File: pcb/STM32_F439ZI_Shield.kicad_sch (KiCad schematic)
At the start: 7 parts, among them U1 Opamp_Dual

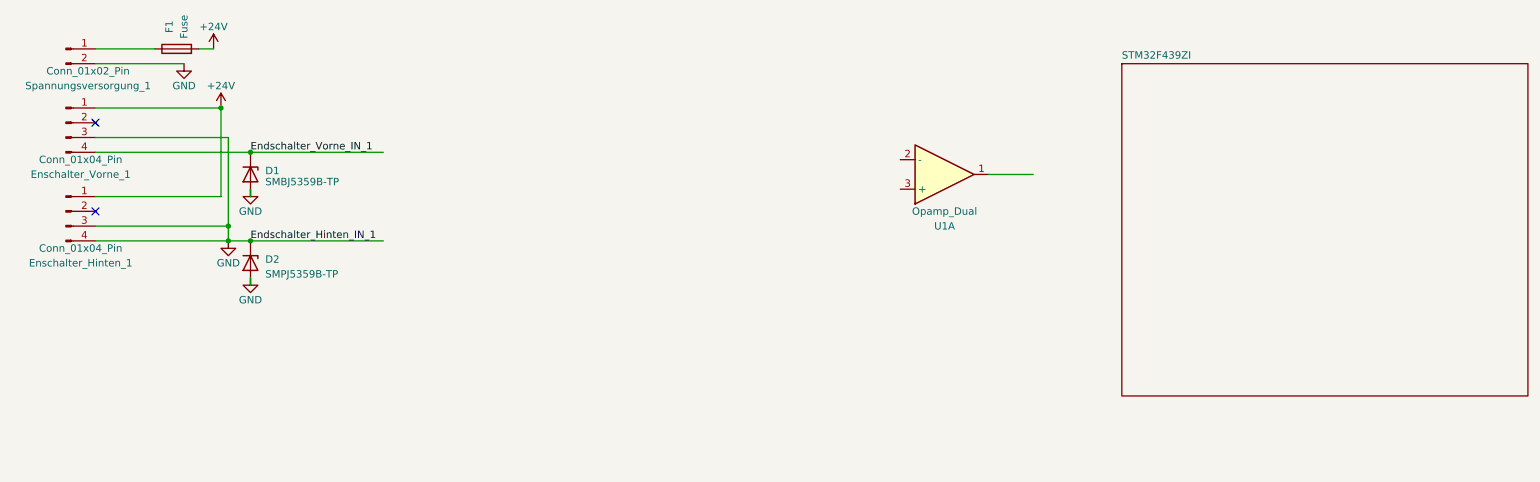
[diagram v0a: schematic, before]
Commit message: added Subsheets vor different component types
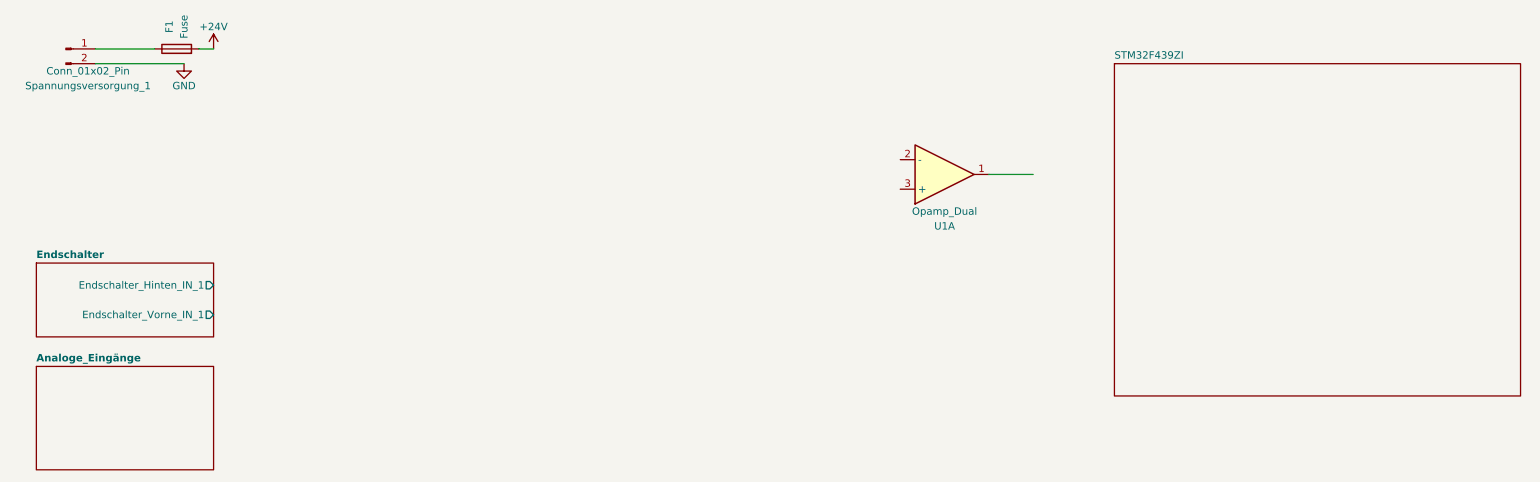
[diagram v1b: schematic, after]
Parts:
- removed D1: SMBJ5359B-TP, Diode_SMD:D_SMB, symbol Diode:Z2SMBxxx
- removed D2: SMPJ5359B-TP, Diode_SMD:D_SMB, symbol Diode:Z2SMBxxx
- removed Enschalter_Hinten_1, Enschalter_Vorne_1: Conn_01x04_Pin, symbol Connector:Conn_01x04_Pin
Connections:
- no-connect marks 2 -> 0
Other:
- added sheet Analoge_Eingänge (analog_in.kicad_sch)
- added sheet Endschalter (Endschalter.kicad_sch)

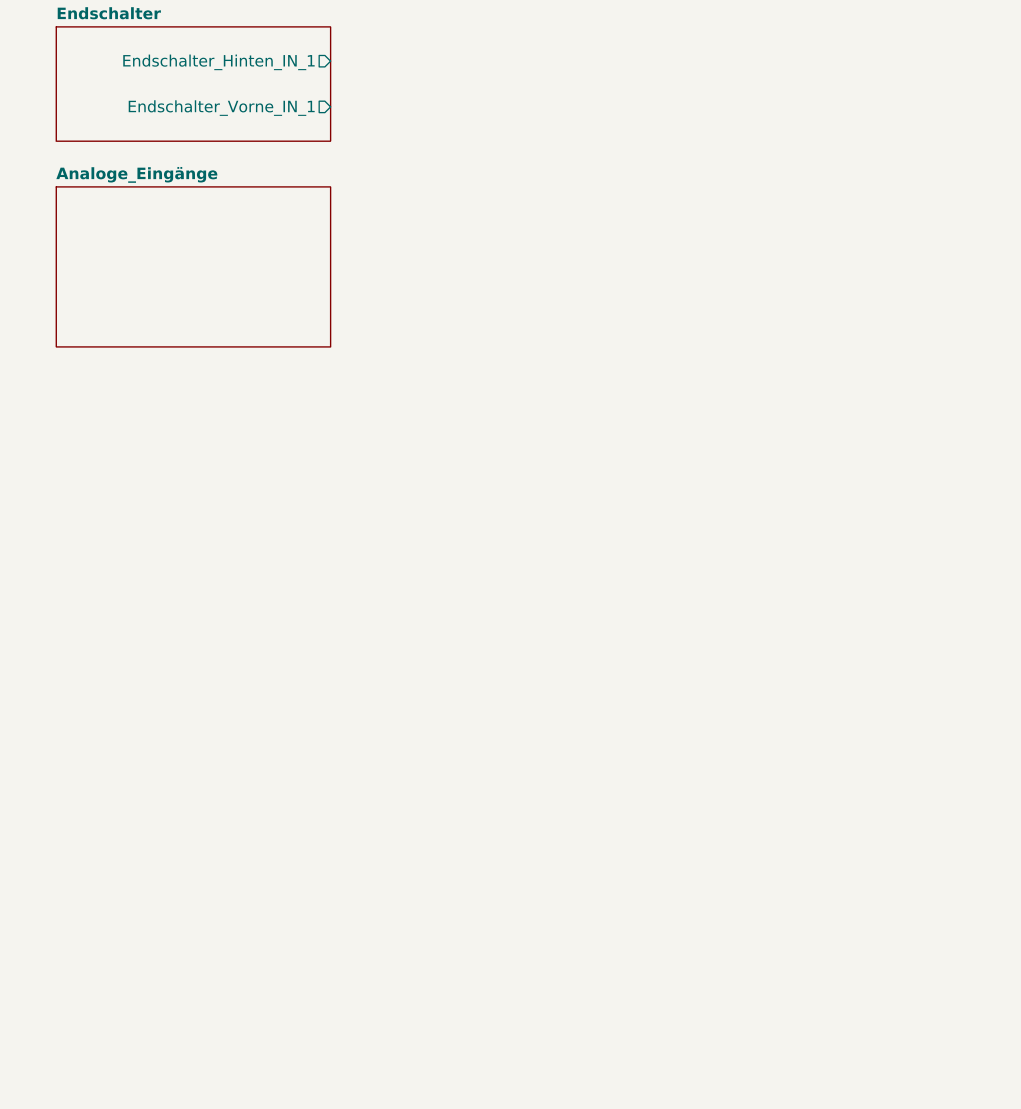
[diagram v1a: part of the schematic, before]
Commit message: added new sheet and added sensors
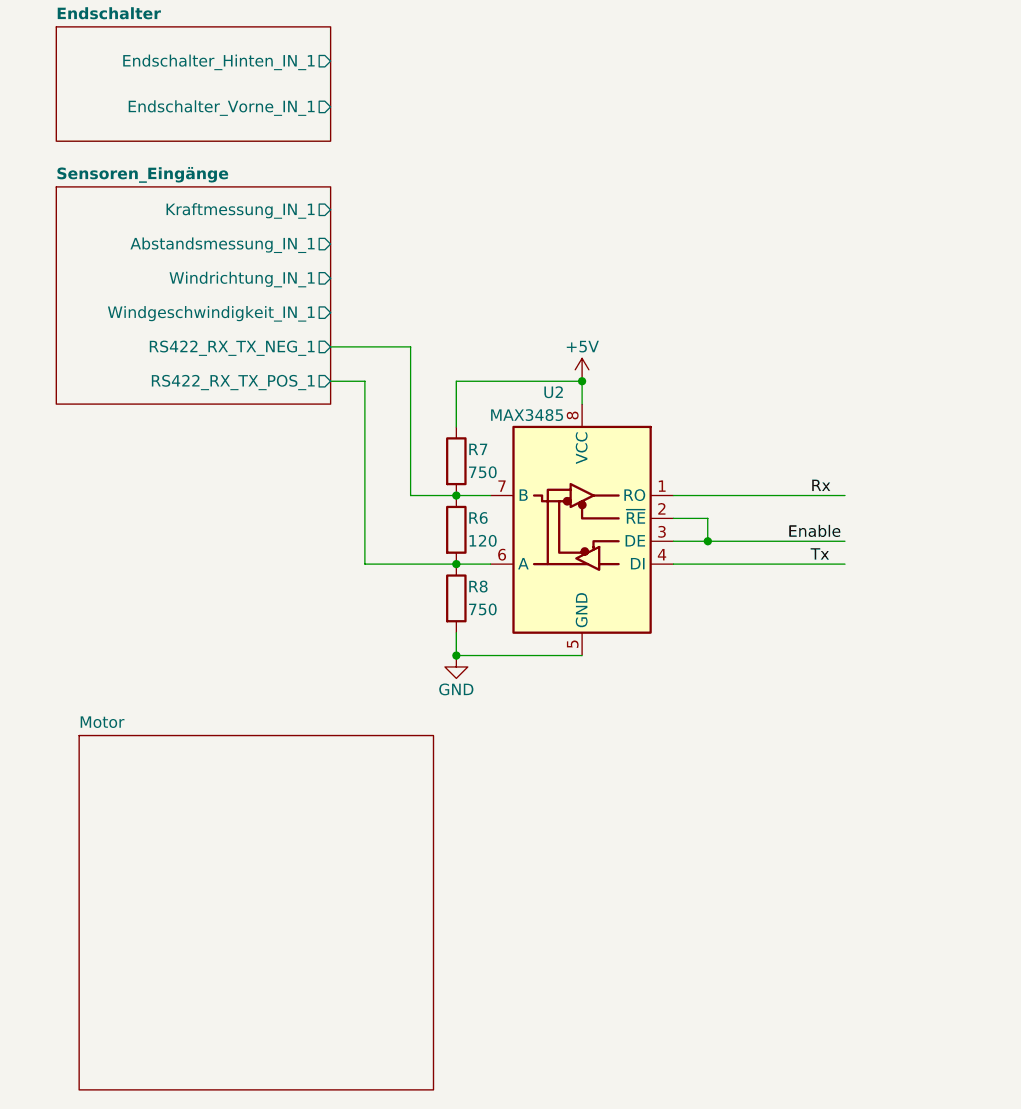
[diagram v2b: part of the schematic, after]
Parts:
- added R6: 120, Resistor_SMD:R_0201_0603Metric, symbol Device:R
- added R7, R8: 750, Resistor_SMD:R_0201_0603Metric, symbol Device:R
- added U2: MAX3485, symbol Interface_UART:MAX3485
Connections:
- net GND: now also R8.2, U2.5 (GND)
- new net +5V: R7.1, U2.8 (VCC)
- new net Enable: U2.2 (~{RE}), U2.3 (DE)
- new net Rx: U2.1 (RO)
- new net Sensoren_Eingänge/RS422_RX_TX_NEG_1: R6.1, R7.2, U2.7 (B)
- new net Sensoren_Eingänge/RS422_RX_TX_POS_1: R6.2, R8.1, U2.6 (A)
- new net Tx: U2.4 (DI)
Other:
- sheet Analoge_Eingänge renamed Sensoren_Eingänge
- added sheet Motor (Motor.kicad_sch)
- sheet Sensoren_Eingänge ports: added Abstandsmessung_IN_1, Kraftmessung_IN_1, RS422_RX_TX_NEG_1, RS422_RX_TX_POS_1, Windgeschwindigkeit_IN_1, Windrichtung_IN_1; removed none

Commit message: Updated PCB
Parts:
- removed U1: Opamp_Dual, symbol Device:Opamp_Dual
- added C1: 22u, Capacitor_SMD:C_0603_1608Metric, symbol Device:C_Small
- added K1, K2: G6S-2, Relay_SMD:Relay_DPDT_Omron_G6S-2F, symbol Relay:G6S-2
- added R10: 240, Resistor_SMD:R_0603_1608Metric, symbol Device:R
- added R9: 10k, Resistor_SMD:R_0201_0603Metric, symbol Device:R
- added U1: LM2904, symbol Amplifier_Operational:LM2904
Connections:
- net Endschalter/Endschalter_Hinten_IN_1: now also K1.1
- net Endschalter/Endschalter_Vorne_IN_1: now also K2.1
- net GND: now also C1.2, K1.12, K2.12, R9.2, U1.4 (V-)
- net Sensoren_Eingänge/RS422_RX_TX_NEG_1 renamed Sensoren_Eingänge/RS485_RX_TX_NEG_1
- net Sensoren_Eingänge/RS422_RX_TX_POS_1 renamed Sensoren_Eingänge/RS485_RX_TX_POS_1
- new net: C1.1, R10.1, U1.3 (+)
- new net +3.3V: U1.8 (V+)
- new net Motor/Drehzahl_Analog_OUT: R9.1, U1.1, U1.2 (-)
- new net Optokoppler/IN0_MCU_IN: K2.4
- new net Optokoppler/IN1_MCU_IN: K1.4
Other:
- added sheet Optokoppler (untitled.kicad_sch)
- sheet Motor ports: added Drehzahl_Analog_OUT, IN0_OUT, IN1_OUT, IN2_OUT, IN3_OUT, OUT1_IN, OUT2_IN, OUT3_IN; removed none
- sheet Sensoren_Eingänge ports: added RS485_RX_TX_NEG_1, RS485_RX_TX_POS_1; removed RS422_RX_TX_NEG_1, RS422_RX_TX_POS_1

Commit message: updated pcb
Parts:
- added C2, C3, C4, C5, C6: 100p, Capacitor_SMD:C_0603_1608Metric, symbol Device:C_Small
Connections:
- net GND: now also C2.2, C3.2, C4.2, C5.2, C6.2
- net STM32F439ZI/IN0_MCU: now reaches K2.3
- net STM32F439ZI/IN1_MCU: now reaches K1.3
- net STM32F439ZI/Drehzahl_Analog_OUT: now reaches R10.2
- new net Motor/Stromsensor_MCU: C6.1
- new net STM32F439ZI/Abstandsmessung_MCU: C3.1
- new net STM32F439ZI/Kraftmessung_MCU: C2.1
- new net STM32F439ZI/Windgeschwindigkeit_MCU: C4.1
- new net STM32F439ZI/Windrichtung_MCU: C5.1
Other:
- sheet Motor ports: added Stromsensor_MCU; removed none
- sheet STM32F439ZI ports: added Abstandsmessung_MCU, Drehzahl_Analog_OUT, Endschalter_Hinten_MCU, Endschalter_Vorne_MCU, IN0_MCU, IN1_MCU, IN2_MCU, IN3_MCU, Kraftmessung_MCU, OUT1_MCU, OUT2_MCU, OUT3_MCU, Strommessung_MCU, UART_EN, UART_RX, UART_TX, Windgeschwindigkeit_MCU, Windrichtung_MCU; removed none
- moved on the sheet: C1, R10, R9, U1A, U1C

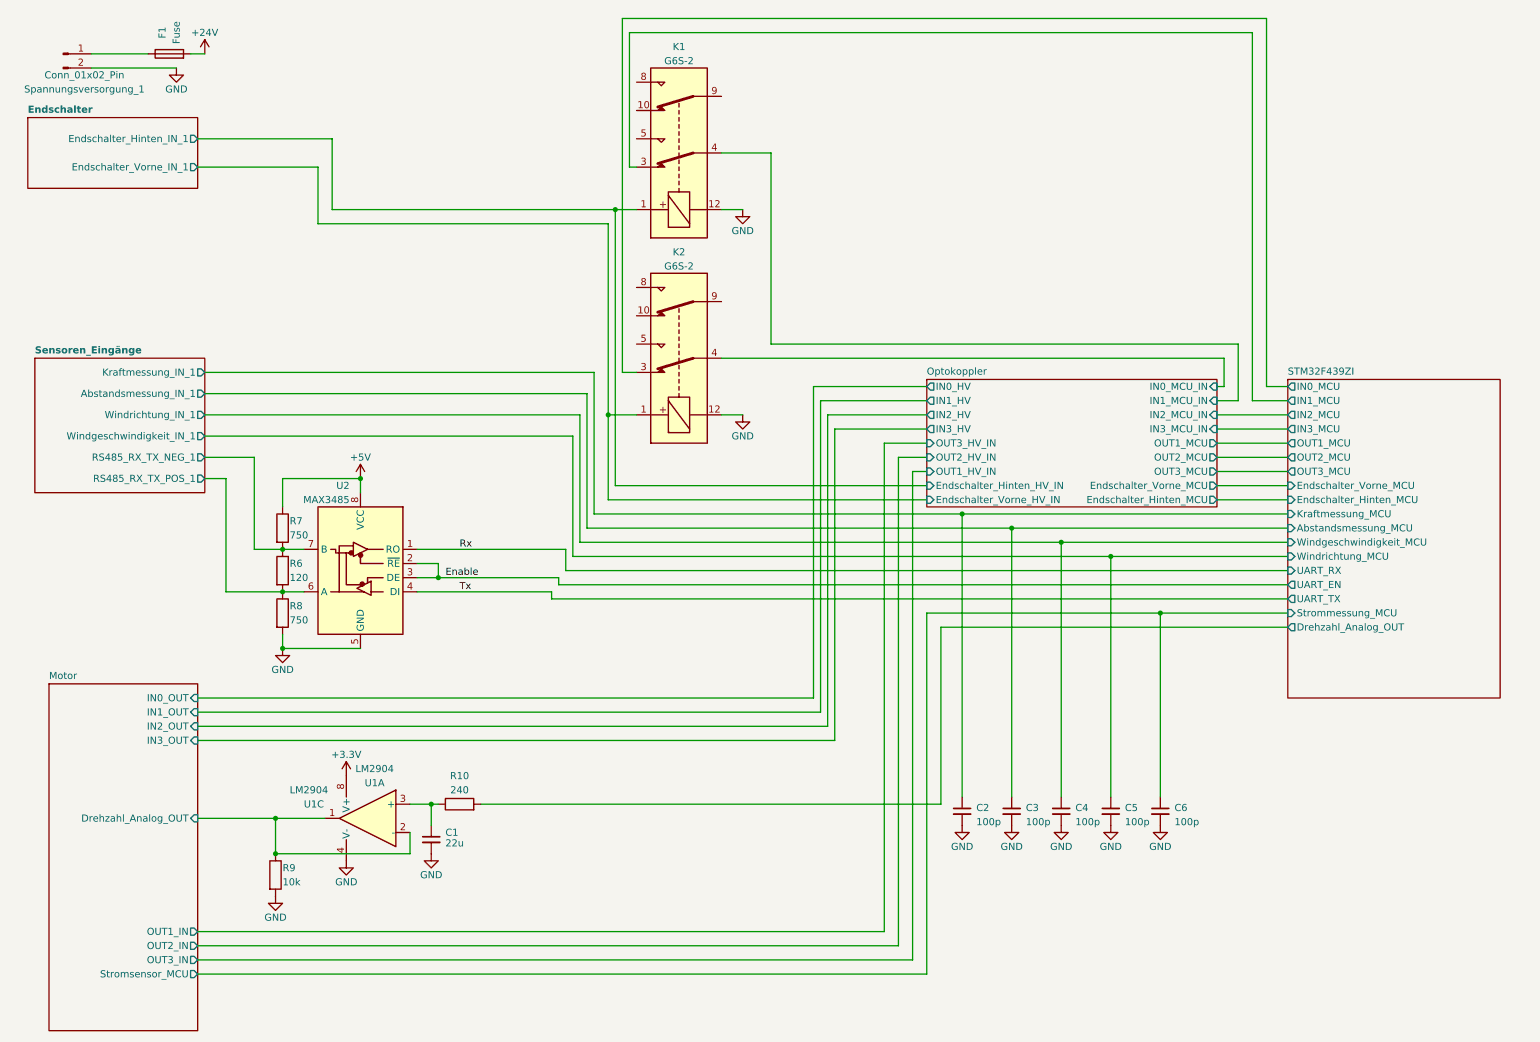
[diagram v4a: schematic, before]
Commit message: add dc/dc converter
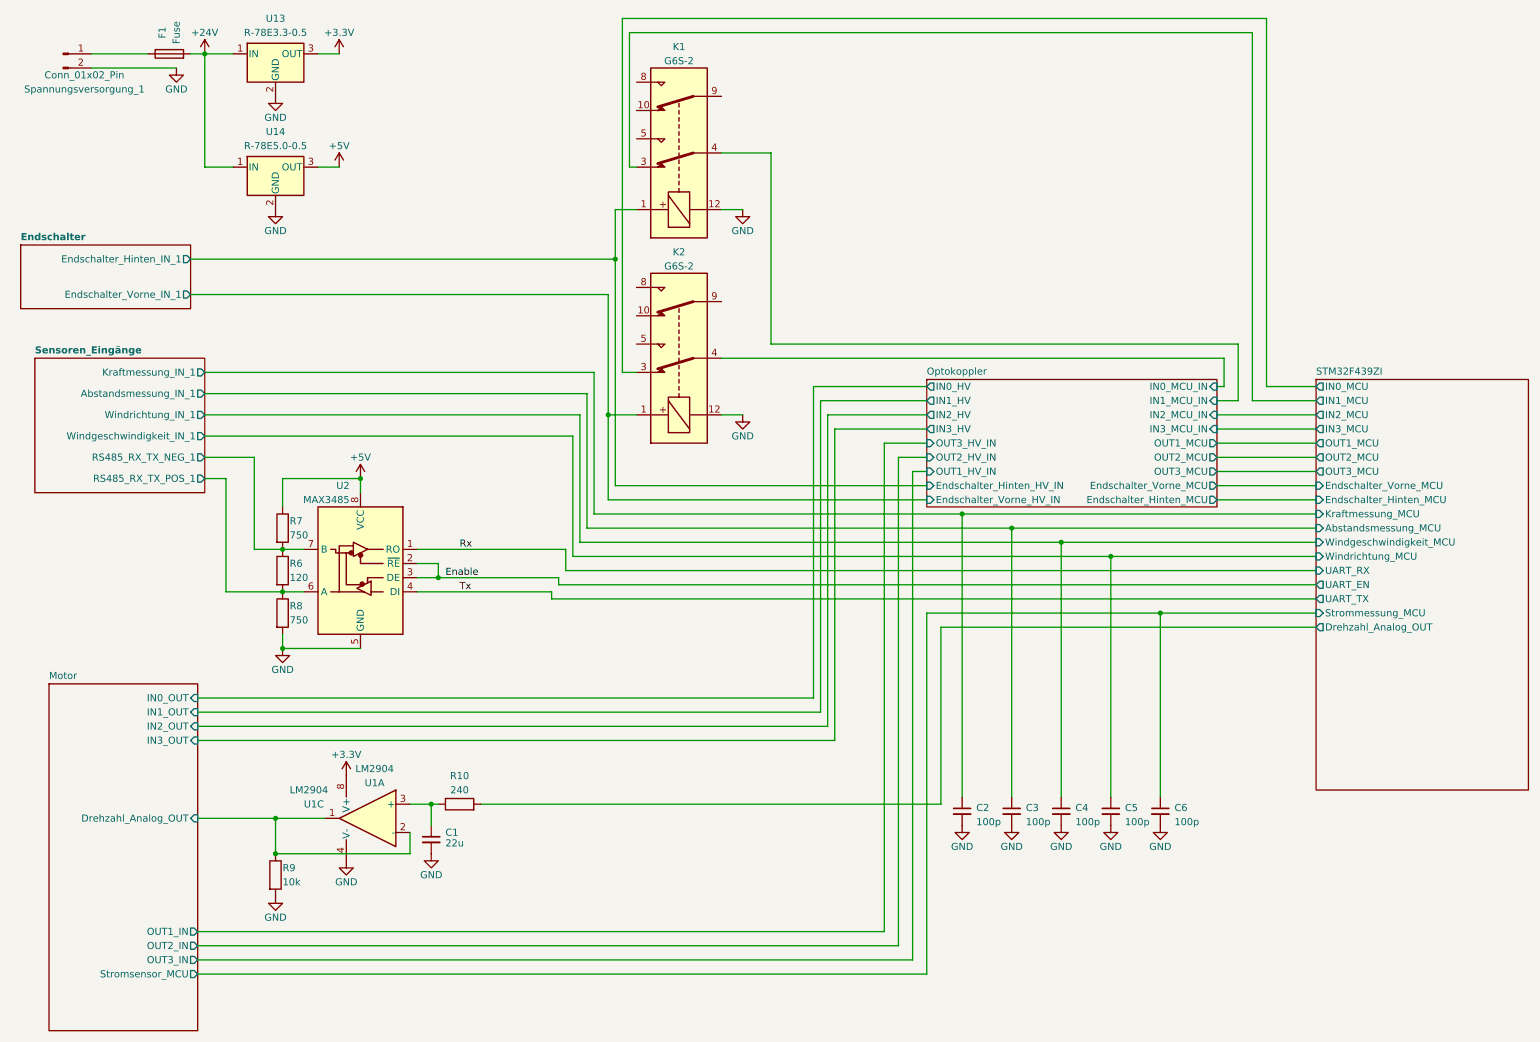
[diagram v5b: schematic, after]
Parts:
- added U13: R-78E3.3-0.5, Converter_DCDC:Converter_DCDC_RECOM_R-78E-0.5_THT, symbol Regulator_Switching:R-78E3.3-0.5
- added U14: R-78E5.0-0.5, Converter_DCDC:Converter_DCDC_RECOM_R-78E-0.5_THT, symbol Regulator_Switching:R-78E5.0-0.5
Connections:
- net +24V: now also U13.1 (IN), U14.1 (IN)
- net +3.3V: now also U13.3 (OUT)
- net +5V: now also U14.3 (OUT)
- net GND: now also U13.2 (GND), U14.2 (GND)
